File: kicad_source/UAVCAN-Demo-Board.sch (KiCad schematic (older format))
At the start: 38 parts, among them CN1 ARDUINO_NANO_33, CN2 691322310004, CN3 GH_SM04B-GHS-TB, CN4 GH_SM04B-GHS-TB, CN5 691322310004, CN6 691322310004, SW1 TAST_VER, U1 MCP2515, U2 SN65VHD232, U3 DS18B20, Y1 16 MHz

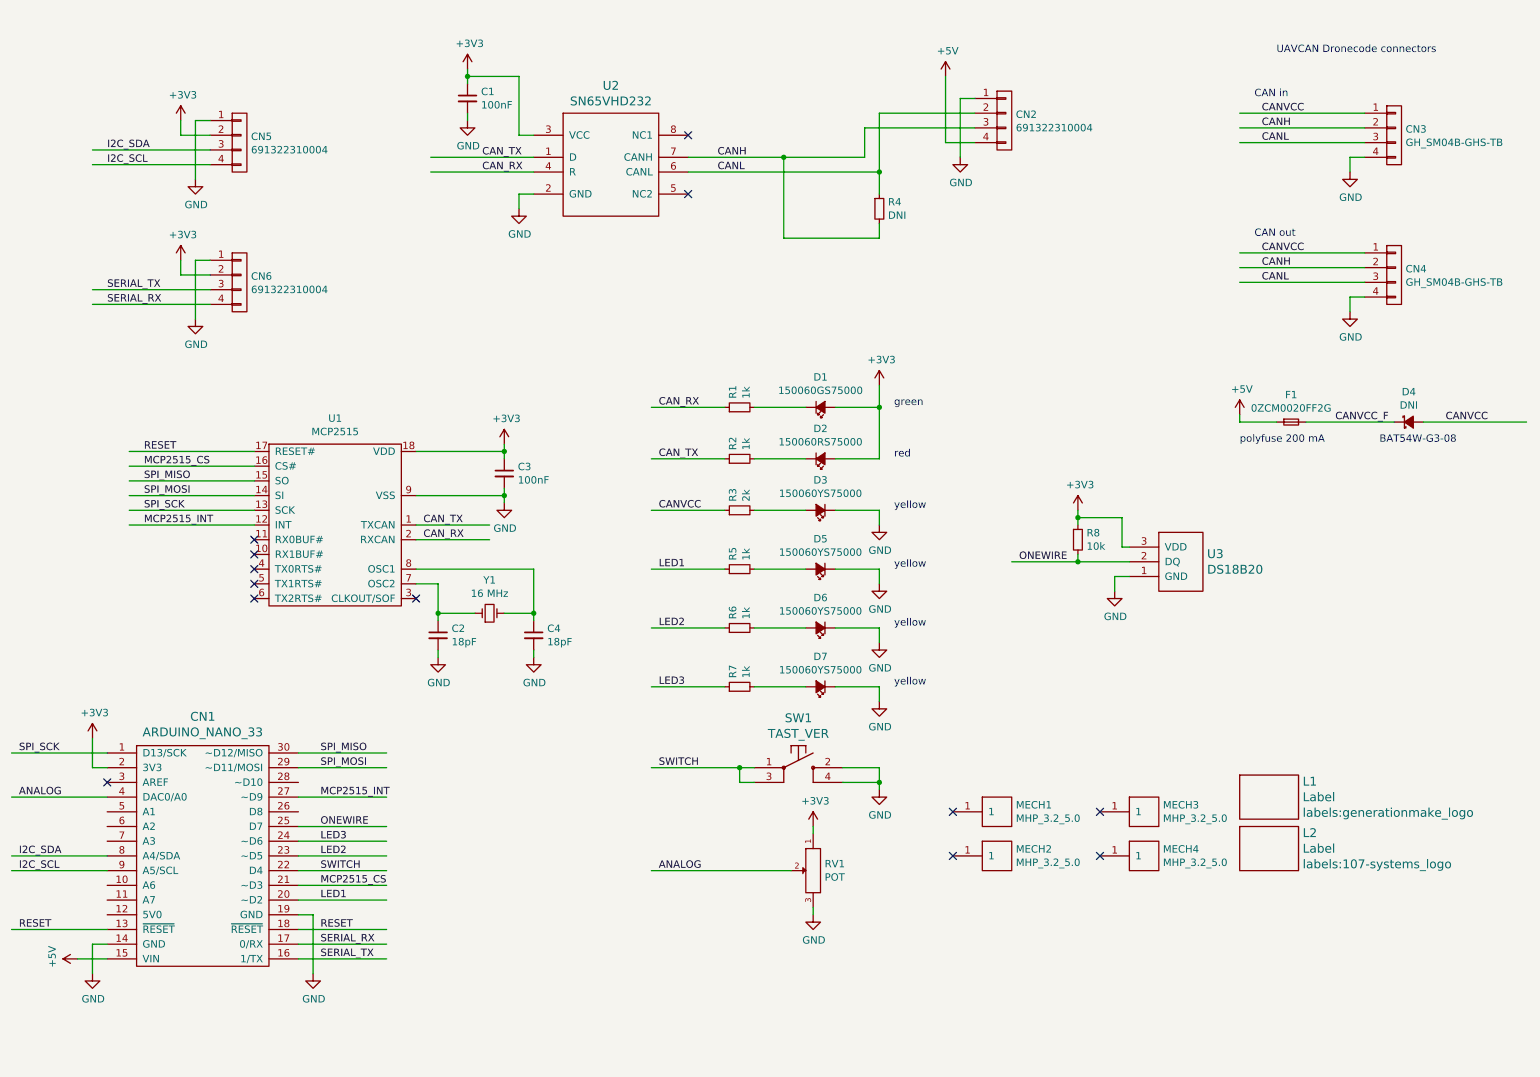
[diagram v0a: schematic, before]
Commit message: updated schematic and layout, added dip switch for configuration, added measurement for CANVCC
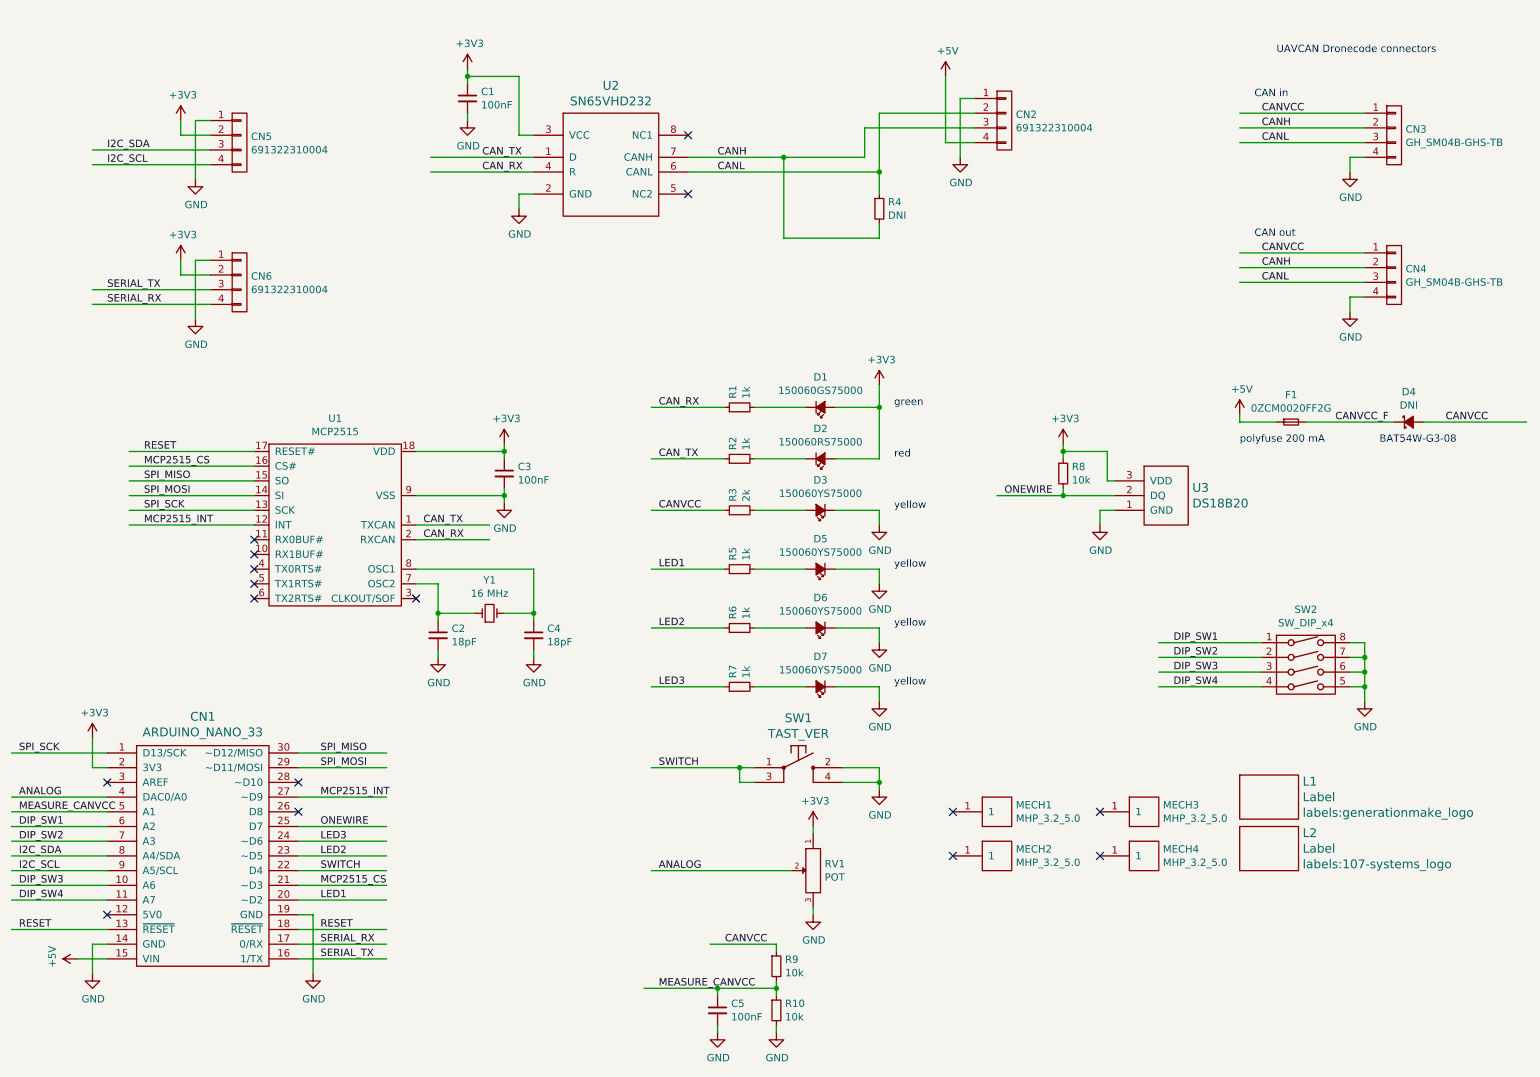
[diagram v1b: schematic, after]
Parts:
- added C5: 100nF, Capacitor_THT:C_Disc_D3.8mm_W2.6mm_P2.50mm, symbol devices:C_Small
- added R10, R9: 10k, Resistor_THT:R_Axial_DIN0207_L6.3mm_D2.5mm_P7.62mm_Horizontal, symbol devices:R_0603
- added SW2: SW_DIP_x4, mechanical-switches:dip_4-300, symbol mechanical-switches:SW_DIP_x4
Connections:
- net labels added: DIP_SW1, DIP_SW2, DIP_SW3, DIP_SW4, MEASURE_CANVCC
- wire segments 144 -> 170
- no-connect marks 13 -> 16
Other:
- moved on the sheet: R8, U3

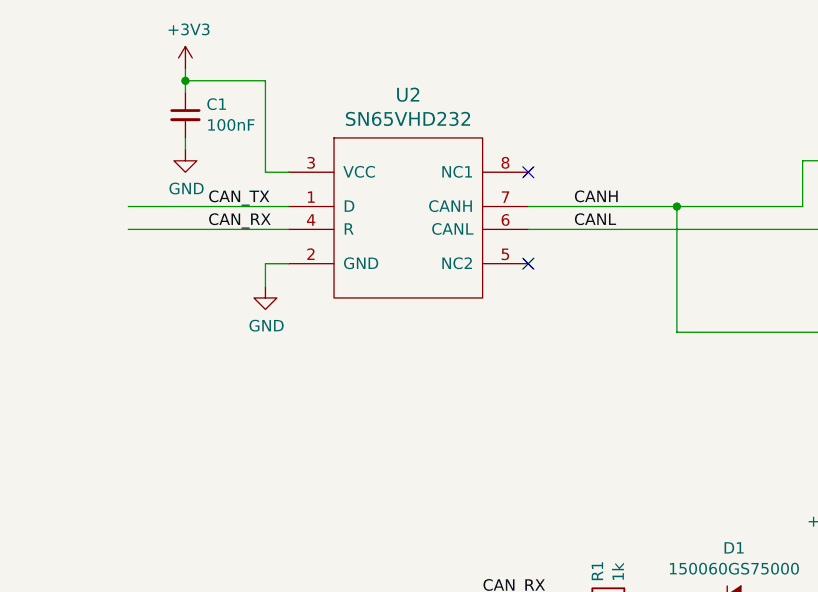
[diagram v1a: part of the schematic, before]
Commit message: switched CAN transceiver to MCP2562 because of DIP package
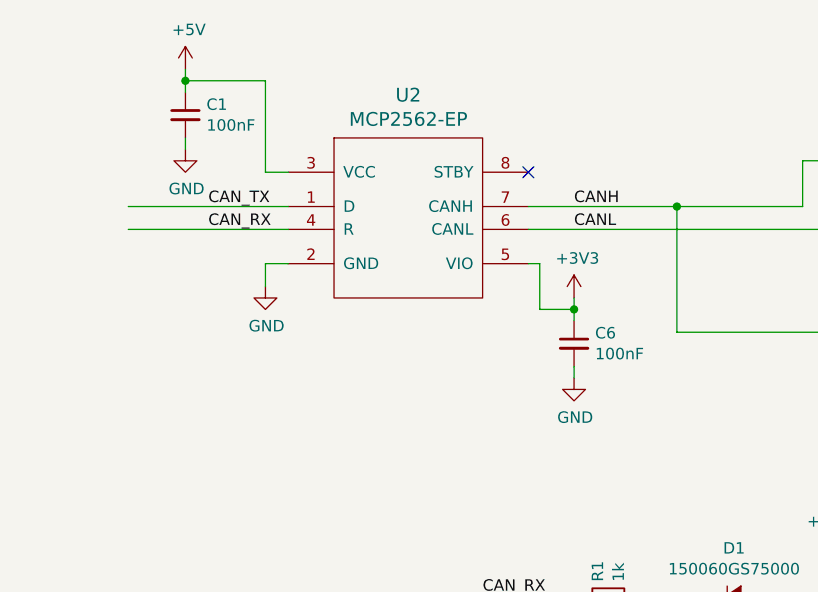
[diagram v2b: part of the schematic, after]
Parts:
- removed U2: SN65VHD232, DIP:DIP-8_W7.62mm, symbol CAN-transceiver:SN65HVD232
- added C6: 100nF, Capacitor_THT:C_Disc_D3.8mm_W2.6mm_P2.50mm, symbol devices:C_0603
- added U2: MCP2562-EP, DIP:DIP-8_W7.62mm, symbol CAN-transceiver:MCP2562-EP
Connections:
- wire segments 170 -> 176
- no-connect marks 16 -> 15
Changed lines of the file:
@@
 Sheet 1 1
 Title "UAVCAN-Demo-Board"
-Date "2021-04-02"
+Date "2021-04-17"
 Rev "0.1"
 Comp "generationmake"
@@
 $EndComp
 $Comp
-L CAN-transceiver:SN65HVD232 U?
-U 1 1 5FD751FF
-P 4250 2000
-AR Path="/5FD58A5B/5FD751FF" Ref="U?"  Part="1"
-AR Path="/5FD751FF" Ref="U2"  Part="1"
-F 0 "U2" H 4775 2887 60  0000 C CNN
-F 1 "SN65VHD232" H 4775 2781 60  0000 C CNN
-F 2 "DIP:DIP-8_W7.62mm" H 5100 1950 60  0001 C CNN
-F 3 "" H 4250 2150 60  0000 C CNN
-	1    4250 2000
-	1    0    0    -1
-$EndComp
-$Comp
 L mechanical-connectors:CONN_01X04 CN?
 U 1 1 5FD75207
@@
 $EndComp
 $Comp
-L power-supply:+3V3 #PWR?
-U 1 1 5FD75219
-P 3800 1000
-AR Path="/5FD58A5B/5FD75219" Ref="#PWR?"  Part="1"
-AR Path="/5FD75219" Ref="#PWR04"  Part="1"
-F 0 "#PWR04" H 3800 850 50  0001 C CNN
-F 1 "+3V3" H 3815 1173 50  0000 C CNN
-F 2 "" H 3800 1000 50  0000 C CNN
-F 3 "" H 3800 1000 50  0000 C CNN
-	1    3800 1000
-	1    0    0    -1
-$EndComp
-$Comp
 L power-supply:GND #PWR?
 U 1 1 5FD7521F
@@
 Wire Wire Line
 	4150 1850 4150 1950
-NoConn ~ 5300 1850
 NoConn ~ 5300 1450
 Text Label 5500 1600 0    50   ~ 0
@@
 Text Label 750  6650 0    50   ~ 0
 DIP_SW4
+$Comp
+L CAN-transceiver:MCP2562-EP U2
+U 1 1 607B4627
+P 4250 2000
+F 0 "U2" H 4775 2887 60  0000 C CNN
+F 1 "MCP2562-EP" H 4775 2781 60  0000 C CNN
+F 2 "DIP:DIP-8_W7.62mm" H 5100 1950 60  0001 C CNN
+F 3 "" H 4250 2150 60  0000 C CNN
+	1    4250 2000
+	1    0    0    -1
+$EndComp
+$Comp
+L devices:C_0603 C?
+U 1 1 607B62E8
+P 5500 2200
+AR Path="/5FD58A5B/607B62E8" Ref="C?"  Part="1"
+AR Path="/607B62E8" Ref="C6"  Part="1"
+F 0 "C6" H 5592 2246 50  0000 L CNN
+F 1 "100nF" H 5592 2155 50  0000 L CNN
+F 2 "Capacitor_THT:C_Disc_D3.8mm_W2.6mm_P2.50mm" H 5500 2050 50  0001 C CNN
+F 3 "" H 5500 2200 50  0000 C CNN
+	1    5500 2200
+	1    0    0    -1
+$EndComp
+$Comp
+L power-supply:+3V3 #PWR?
+U 1 1 607B6554
+P 5500 2000
+AR Path="/5FD58A5B/607B6554" Ref="#PWR?"  Part="1"
+AR Path="/607B6554" Ref="#PWR0102"  Part="1"
+F 0 "#PWR0102" H 5500 1850 50  0001 C CNN
+F 1 "+3V3" H 5515 2173 50  0000 C CNN
+F 2 "" H 5500 2000 50  0000 C CNN
+F 3 "" H 5500 2000 50  0000 C CNN
+	1    5500 2000
+	1    0    0    -1
+$EndComp
+$Comp
+L power-supply:GND #PWR?
+U 1 1 607B655E
+P 5500 2350
+AR Path="/5FD58A5B/607B655E" Ref="#PWR?"  Part="1"
+AR Path="/607B655E" Ref="#PWR0103"  Part="1"
+F 0 "#PWR0103" H 5500 2100 50  0001 C CNN
+F 1 "GND" H 5505 2177 50  0000 C CNN
+F 2 "" H 5500 2350 50  0000 C CNN
+F 3 "" H 5500 2350 50  0000 C CNN
+	1    5500 2350
+	1    0    0    -1
+$EndComp
+Wire Wire Line
+	5500 2300 5500 2350
+Wire Wire Line
+	5500 2000 5500 2050
+$Comp
+L power-supply:+5V #PWR?
+U 1 1 607C20B1
+P 3800 1000
+AR Path="/5FD58A5B/607C20B1" Ref="#PWR?"  Part="1"
+AR Path="/607C20B1" Ref="#PWR0104"  Part="1"
+F 0 "#PWR0104" H 3800 850 50  0001 C CNN
+F 1 "+5V" H 3815 1173 50  0000 C CNN
+F 2 "" H 3800 1000 50  0000 C CNN
+F 3 "" H 3800 1000 50  0000 C CNN
+	1    3800 1000
+	1    0    0    -1
+$EndComp
+Wire Wire Line
+	5500 2050 5350 2050
+Wire Wire Line
+	5350 2050 5350 1850
+Wire Wire Line
+	5350 1850 5300 1850
+Connection ~ 5500 2050
+Wire Wire Line
+	5500 2050 5500 2100
 $EndSCHEMATC

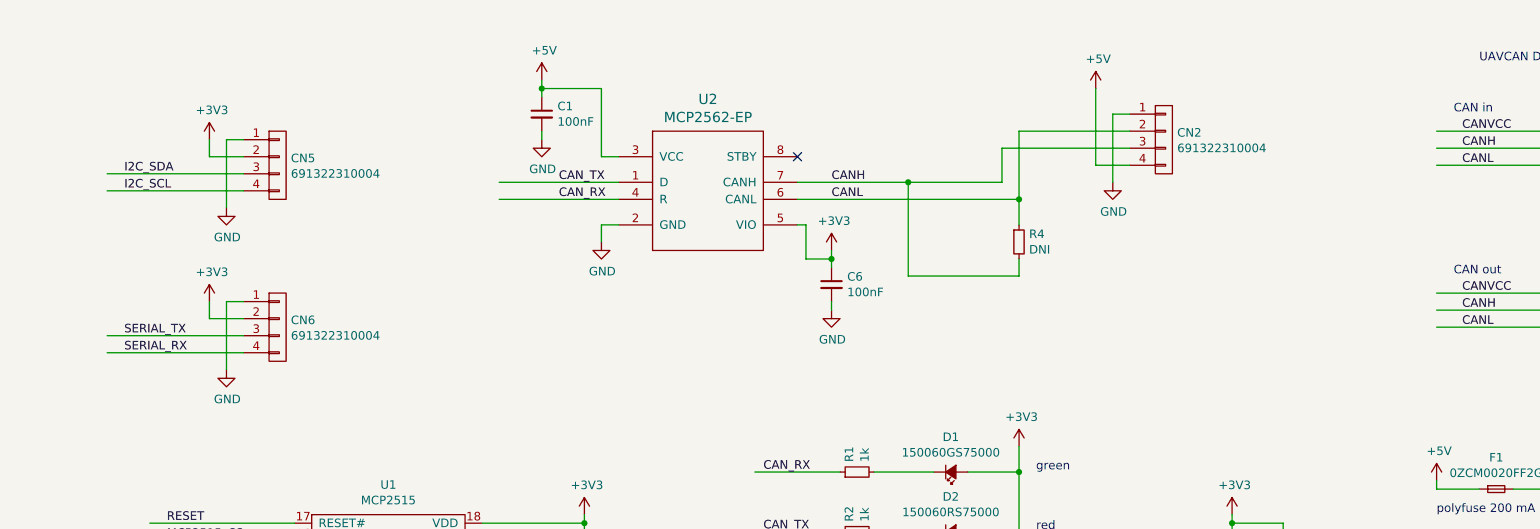
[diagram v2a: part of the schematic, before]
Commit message: added Qwiic connector
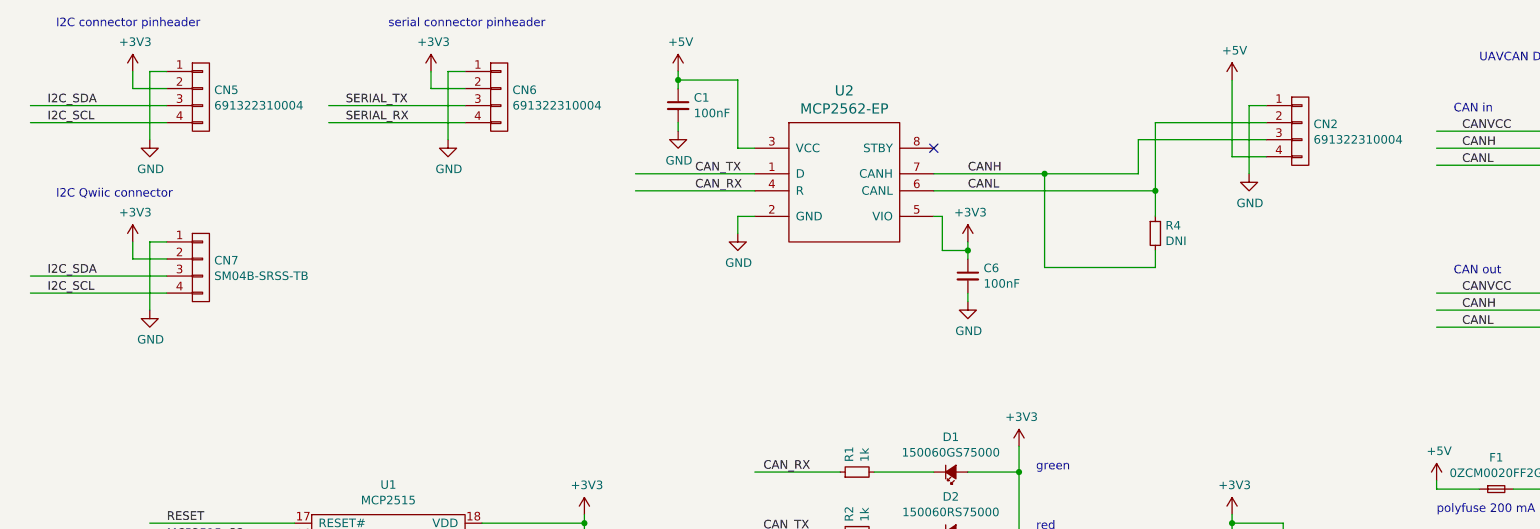
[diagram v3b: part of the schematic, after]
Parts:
- added CN7: SM04B-SRSS-TB, Connector_JST:JST_SH_SM04B-SRSS-TB_1x04-1MP_P1.00mm_Horizontal, symbol mechanical-connectors:CONN_01X04
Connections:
- wire segments 176 -> 182
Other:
- note added: "I2C Qwiic connector"
- note added: "I2C connector pinheader"
- note added: "serial connector pinheader"
- moved on the sheet: C1, C6, CN2, CN5, CN6, R4, U2
